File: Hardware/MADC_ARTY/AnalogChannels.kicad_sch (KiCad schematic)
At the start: 37 parts, among them Q1 MMBT6429, Q10 MMBF4392, Q11 MMBT6429, Q12 MMBT6429, Q2 JFE2140D, Q3 MMBT6429, Q4 MMBF4392, Q5 MMBT6429, Q6 MMBT6429, Q7 MMBT6429, Q8 JFE2140D, Q9 MMBT6429, U2 ADA4077-4ARUZ, U3 ADA4077-4ARUZ, U4 ADA4077-2xRMZ

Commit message: Schematic
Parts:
- removed RN1, RN2: MPMT4001AT1, Package_TO_SOT_SMD:SOT-23, symbol Device:VoltageDivider
- added RN1, RN2: MPMT4001AT1, Package_TO_SOT_SMD:SOT-23, symbol Device:VoltageDivider_CenterPin3
- renumbered U2 to U1, U3 to U2, U4 to U3
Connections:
- net at Q9.2 (E), R11.1, R9.1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: now also RN2.2
- net at R11.2, R12.2, R13.1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: now also RN2.3
- net at R4.2, R5.2, R6.1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: now also RN1.3
- net at Q11.2 (E), R13.2, R14.1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: now also RN2.1
- net at Q3.2 (E), R2.1, R4.1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: now also RN1.2
- net at Q5.2 (E), R6.2, R7.1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: now also RN1.1

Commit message: Schematic
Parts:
- removed U1, U2: ADA4077-4ARUZ, Package_SO:TSSOP-14_4.4x5mm_P0.65mm, symbol MADC_ARTY:ADA4077-4ARUZ
- removed U3: ADA4077-2xRMZ, Package_SO:MSOP-8_3x3mm_P0.65mm, symbol MADC_ARTY:ADA4077-2xRMZ
- added U1: OPA2192, Package_SO:VSSOP-8_3x3mm_P0.65mm, symbol Amplifier_Operational:OPA2197xDGK
- added U2, U3: OPA4192IPW, Package_SO:TSSOP-14_4.4x5mm_P0.65mm, symbol Amplifier_Operational:OPA4196xPW
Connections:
- net GND: now also U1.3 (+), U1.5 (+)
- net OUT_N: now also U3.8
- net OUT_P: now also U2.8
- net at Q1.3 (C), Q2.1, Q3.3 (C): now also U2.10 (+), U2.12 (+)
- net at Q11.2 (E), R13.2, R14.1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: now also U3.6 (-)
- net at Q9.2 (E), R11.1, R9.1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: now also U3.2 (-)
- net at R11.2, R12.2, R13.1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: now also U1.7
- net at Q10.3 (G): now also U3.13 (-), U3.14
- net at R4.2, R5.2, R6.1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: now also U1.1
- net at R1.2, R3.1: now also U1.2 (-)
- net at Q11.3 (C), Q12.3 (C), Q8.5: now also U3.9 (-)
- net at R10.2, R12.1: now also U3.3 (+), U3.5 (+)
- net at Q12.1 (B): now also U3.7
- net at Q1.1 (B): now also U2.1
- net at Q3.2 (E), R2.1, R4.1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: now also U2.2 (-)
- net at R3.2, R5.1: now also U2.3 (+), U2.5 (+)
- net at R10.1, R8.2: now also U1.6 (-)
- net at Q2.5, Q5.3 (C), Q6.3 (C): now also U2.9 (-)
- net at Q5.2 (E), R6.2, R7.1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: now also U2.6 (-)
- net at Q4.3 (G): now also U2.13 (-), U2.14
- net at Q6.1 (B): now also U2.7
- net at Q7.3 (C), Q8.1, Q9.3 (C): now also U3.10 (+), U3.12 (+)
- net at Q7.1 (B): now also U3.1
- net VCC renamed +18V
- net +18V: now also U1.8 (V+), U2.4 (V+), U3.4 (V+)
- net VEE renamed -18V
- net -18V: now also U1.4 (V-), U2.11 (V-), U3.11 (V-)

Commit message: Schematic
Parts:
- added unit 3 of Q8
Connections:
- no-connect marks 2 -> 4
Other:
- moved on the sheet: C1, C2, C3, C4, C5, C6, Q2C, U2E, U3E

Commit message: PCB and Schematic
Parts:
- removed C1, C4: 0.1u, Capacitor_SMD:C_0603_1608Metric, symbol Device:C
- removed Q10: MMBF4392, Package_TO_SOT_SMD:SOT-23, symbol Transistor_FET:MMBF4392
- removed Q11, Q12, Q7, Q9: MMBT6429, Package_TO_SOT_SMD:SOT-23, symbol Transistor_BJT:Q_NPN_BEC
- removed Q8: JFE2140D, Package_SO:SOIC-8_3.9x4.9mm_P1.27mm, symbol Transistor_FET:JFE2140D
- removed R10, R14, R9: 21k5/0.125W, Resistor_SMD:R_0603_1608Metric, symbol Device:R
- removed R11, R12, R13: 2k/0.1%, Resistor_SMD:R_0603_1608Metric, symbol Device:R
- removed RN2: MPMT4001AT1, Package_TO_SOT_SMD:SOT-23, symbol Device:VoltageDivider_CenterPin3
- removed U3: OPA4192IPW, Package_SO:TSSOP-14_4.4x5mm_P0.65mm, symbol Amplifier_Operational:OPA4196xPW
- added R3, R5: 0, Resistor_SMD:R_0603_1608Metric, symbol Device:R
- added TP19, TP21, TP23, TP25, TP27: TestPoint, symbol Connector:TestPoint
- R8: value 14k7 -> 0
- renumbered C2 to C1, C3 to C2, C5 to C3, C6 to C4, Q2 to Q1, Q1 to Q2, R7 to R10, R3 to R4, R4 to R6, R5 to R7, R6 to R9
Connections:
- net +10V: no longer R8.1
- net at Q1.1, Q2.3 (C), Q3.3 (C)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: now also TP21.1
- net at Q1.2, Q1.6, Q4.2 (S): now also TP19.1
- net at U1.7: now also R8.2, R5.2
- net at U1.6 (-): now also R3.2, R5.1; no longer R8.2
- net at R6.2, R7.2, R9.1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: now also R8.1, TP27.1
- net at R1.2, R4.1, U1.2 (-): now also R3.1
- net IN_P renamed IN
- net IN: now also TP25.1
- net OUT_P renamed OUT
- net OUT: now also TP23.1
- no-connect marks 4 -> 2
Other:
- moved on the sheet: C1, C2, C3, C4, Q1A, Q1B, Q1C, Q2, Q3, Q4, Q5, Q6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

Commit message: PCB
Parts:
- TP1: renamed from TP25; footprint (none) -> TestPoint:TestPoint_Pad_D2.0mm
- TP2: renamed from TP19; footprint (none) -> TestPoint:TestPoint_Pad_D2.0mm
- TP3: renamed from TP21; footprint (none) -> TestPoint:TestPoint_Pad_D2.0mm
- TP4: renamed from TP27; footprint (none) -> TestPoint:TestPoint_Pad_D2.0mm
- TP5: renamed from TP23; footprint (none) -> TestPoint:TestPoint_Pad_D2.0mm

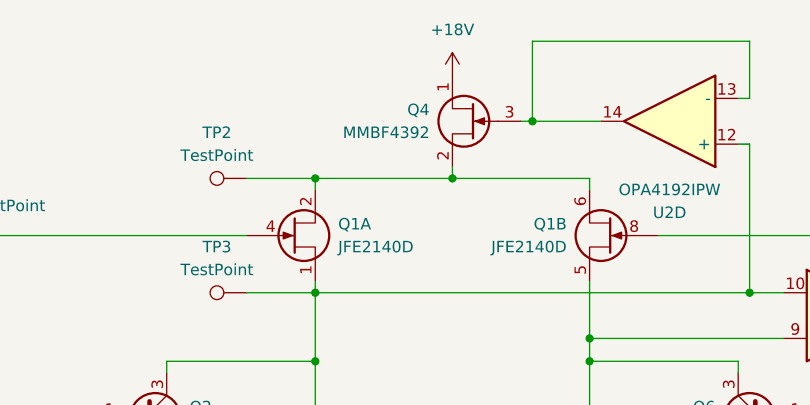
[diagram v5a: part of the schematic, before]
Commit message: MADC module send to production
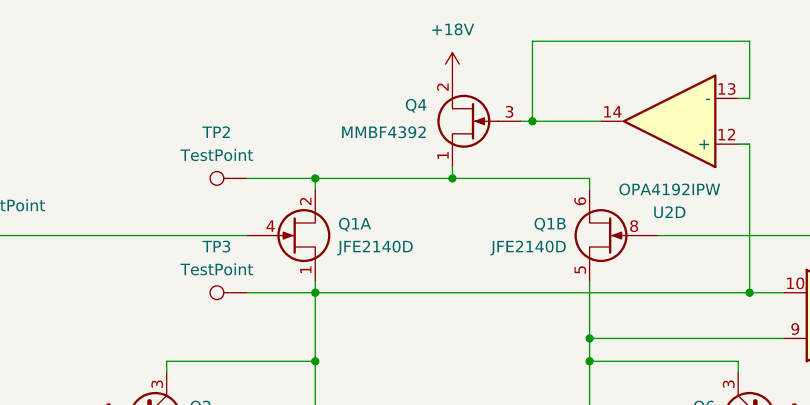
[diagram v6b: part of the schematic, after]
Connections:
- net +18V: now also Q4.2 (S); no longer Q4.1 (D)
- net at Q1.2, Q1.6, TP2.1: now also Q4.1 (D); no longer Q4.2 (S)
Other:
- moved on the sheet: Q4
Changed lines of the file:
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@@
 			(project "MADC_ARTY"
 				(path "/eadab778-ea7c-433e-b0bd-0d0c238907e0/37dfacfc-f3f5-4a09-9e7e-ab0b8ea302f6/3691a135-d759-4453-b099-98c35d021fc0"
-					(reference "#PWR0162")
+					(reference "#PWR0126")
 					(unit 1)
 				)
@@
 			(project "MADC_ARTY"
 				(path "/eadab778-ea7c-433e-b0bd-0d0c238907e0/37dfacfc-f3f5-4a09-9e7e-ab0b8ea302f6/3691a135-d759-4453-b099-98c35d021fc0"
-					(reference "R70")
+					(reference "R57")
 					(unit 1)
 				)
@@
 			(project "MADC_ARTY"
 				(path "/eadab778-ea7c-433e-b0bd-0d0c238907e0/37dfacfc-f3f5-4a09-9e7e-ab0b8ea302f6/3691a135-d759-4453-b099-98c35d021fc0"
-					(reference "TP37")
+					(reference "TP31")
 					(unit 1)
 				)
@@
 			(project "MADC_ARTY"
 				(path "/eadab778-ea7c-433e-b0bd-0d0c238907e0/37dfacfc-f3f5-4a09-9e7e-ab0b8ea302f6/3691a135-d759-4453-b099-98c35d021fc0"
-					(reference "U28")
+					(reference "U20")
 					(unit 3)
 				)
@@
 			(project "MADC_ARTY"
 				(path "/eadab778-ea7c-433e-b0bd-0d0c238907e0/37dfacfc-f3f5-4a09-9e7e-ab0b8ea302f6/3691a135-d759-4453-b099-98c35d021fc0"
-					(reference "R78")
+					(reference "R65")
 					(unit 1)
 				)
@@
 			(project "MADC_ARTY"
 				(path "/eadab778-ea7c-433e-b0bd-0d0c238907e0/37dfacfc-f3f5-4a09-9e7e-ab0b8ea302f6/3691a135-d759-4453-b099-98c35d021fc0"
-					(reference "C66")
+					(reference "C46")
 					(unit 1)
 				)
@@
 			(project "MADC_ARTY"
 				(path "/eadab778-ea7c-433e-b0bd-0d0c238907e0/37dfacfc-f3f5-4a09-9e7e-ab0b8ea302f6/3691a135-d759-4453-b099-98c35d021fc0"
-					(reference "#PWR0161")
+					(reference "#PWR0125")
 					(unit 1)
 				)
@@
 			(project "MADC_ARTY"
 				(path "/eadab778-ea7c-433e-b0bd-0d0c238907e0/37dfacfc-f3f5-4a09-9e7e-ab0b8ea302f6/3691a135-d759-4453-b099-98c35d021fc0"
-					(reference "#PWR0160")
+					(reference "#PWR0124")
 					(unit 1)
 				)
@@
 			(project "MADC_ARTY"
 				(path "/eadab778-ea7c-433e-b0bd-0d0c238907e0/37dfacfc-f3f5-4a09-9e7e-ab0b8ea302f6/3691a135-d759-4453-b099-98c35d021fc0"
-					(reference "R77")
+					(reference "R64")
 					(unit 1)
 				)
@@
 			(project "MADC_ARTY"
 				(path "/eadab778-ea7c-433e-b0bd-0d0c238907e0/37dfacfc-f3f5-4a09-9e7e-ab0b8ea302f6/3691a135-d759-4453-b099-98c35d021fc0"
-					(reference "TP36")
+					(reference "TP30")
 					(unit 1)
 				)
@@
 			(project "MADC_ARTY"
 				(path "/eadab778-ea7c-433e-b0bd-0d0c238907e0/37dfacfc-f3f5-4a09-9e7e-ab0b8ea302f6/3691a135-d759-4453-b099-98c35d021fc0"
-					(reference "TP35")
+					(reference "TP29")
 					(unit 1)
 				)
@@
 			(project "MADC_ARTY"
 				(path "/eadab778-ea7c-433e-b0bd-0d0c238907e0/37dfacfc-f3f5-4a09-9e7e-ab0b8ea302f6/3691a135-d759-4453-b099-98c35d021fc0"
-					(reference "U27")
+					(reference "U19")
 					(unit 3)
 				)
@@
 			(project "MADC_ARTY"
 				(path "/eadab778-ea7c-433e-b0bd-0d0c238907e0/37dfacfc-f3f5-4a09-9e7e-ab0b8ea302f6/3691a135-d759-4453-b099-98c35d021fc0"
-					(reference "#PWR0167")
+					(reference "#PWR0131")
 					(unit 1)
 				)
@@
 			(project "MADC_ARTY"
 				(path "/eadab778-ea7c-433e-b0bd-0d0c238907e0/37dfacfc-f3f5-4a09-9e7e-ab0b8ea302f6/3691a135-d759-4453-b099-98c35d021fc0"
-					(reference "R75")
+					(reference "R62")
 					(unit 1)
 				)
@@
 			(project "MADC_ARTY"
 				(path "/eadab778-ea7c-433e-b0bd-0d0c238907e0/37dfacfc-f3f5-4a09-9e7e-ab0b8ea302f6/3691a135-d759-4453-b099-98c35d021fc0"
-					(reference "RN2")
+					(reference "RN3")
 					(unit 1)
 				)
@@
 	(symbol
 		(lib_id "Transistor_FET:MMBF4392")
-		(at 156.21 35.56 0)
-		(mirror y)
+		(at 156.21 35.56 180)
 		(unit 1)
 		(exclude_from_sim no)
@@
 		(dnp no)
 		(property "Reference" "Q4"
-			(at 151.13 34.2899 0)
+			(at 150.876 33.782 0)
 			(effects
 				(font
@@
 		)
 		(property "Value" "MMBF4392"
-			(at 151.13 36.8299 0)
+			(at 150.876 36.83 0)
 			(effects
 				(font
@@
 		)
 		(property "Footprint" "Package_TO_SOT_SMD:SOT-23"
-			(at 151.13 37.465 0)
+			(at 151.13 33.655 0)
 			(effects
 				(font
@@
 		)
 		(property "Datasheet" "https://www.onsemi.com/pub/Collateral/MMBF4391LT1-D.PDF"
-			(at 151.13 39.37 0)
+			(at 151.13 31.75 0)
 			(effects
 				(font
@@
 			(project "MADC_ARTY"
 				(path "/eadab778-ea7c-433e-b0bd-0d0c238907e0/37dfacfc-f3f5-4a09-9e7e-ab0b8ea302f6/3691a135-d759-4453-b099-98c35d021fc0"
-					(reference "U28")
+					(reference "U20")
 					(unit 5)
 				)
@@
 			(project "MADC_ARTY"
 				(path "/eadab778-ea7c-433e-b0bd-0d0c238907e0/37dfacfc-f3f5-4a09-9e7e-ab0b8ea302f6/3691a135-d759-4453-b099-98c35d021fc0"
-					(reference "#PWR0163")
+					(reference "#PWR0127")
 					(unit 1)
 				)
@@
 			(project "MADC_ARTY"
 				(path "/eadab778-ea7c-433e-b0bd-0d0c238907e0/37dfacfc-f3f5-4a09-9e7e-ab0b8ea302f6/3691a135-d759-4453-b099-98c35d021fc0"
-					(reference "R69")
+					(reference "R56")
 					(unit 1)
 				)
@@
 			(project "MADC_ARTY"
 				(path "/eadab778-ea7c-433e-b0bd-0d0c238907e0/37dfacfc-f3f5-4a09-9e7e-ab0b8ea302f6/3691a135-d759-4453-b099-98c35d021fc0"
-					(reference "#PWR0164")
+					(reference "#PWR0128")
 					(unit 1)
 				)
@@
 			(project "MADC_ARTY"
 				(path "/eadab778-ea7c-433e-b0bd-0d0c238907e0/37dfacfc-f3f5-4a09-9e7e-ab0b8ea302f6/3691a135-d759-4453-b099-98c35d021fc0"
-					(reference "U27")
+					(reference "U19")
 					(unit 2)
 				)
@@
 			(project "MADC_ARTY"
 				(path "/eadab778-ea7c-433e-b0bd-0d0c238907e0/37dfacfc-f3f5-4a09-9e7e-ab0b8ea302f6/3691a135-d759-4453-b099-98c35d021fc0"
-					(reference "TP33")
+					(reference "TP27")
 					(unit 1)
 				)
@@
 			(project "MADC_ARTY"
 				(path "/eadab778-ea7c-433e-b0bd-0d0c238907e0/37dfacfc-f3f5-4a09-9e7e-ab0b8ea302f6/3691a135-d759-4453-b099-98c35d021fc0"
-					(reference "#PWR0157")
+					(reference "#PWR0121")
 					(unit 1)
 				)
@@
 			(project "MADC_ARTY"
 				(path "/eadab778-ea7c-433e-b0bd-0d0c238907e0/37dfacfc-f3f5-4a09-9e7e-ab0b8ea302f6/3691a135-d759-4453-b099-98c35d021fc0"
-					(reference "U28")
+					(reference "U20")
 					(unit 1)
 				)
@@
 			(project "MADC_ARTY"
 				(path "/eadab778-ea7c-433e-b0bd-0d0c238907e0/37dfacfc-f3f5-4a09-9e7e-ab0b8ea302f6/3691a135-d759-4453-b099-98c35d021fc0"
-					(reference "R71")
+					(reference "R58")
 					(unit 1)
 				)
@@
 			(project "MADC_ARTY"
 				(path "/eadab778-ea7c-433e-b0bd-0d0c238907e0/37dfacfc-f3f5-4a09-9e7e-ab0b8ea302f6/3691a135-d759-4453-b099-98c35d021fc0"
-					(reference "TP34")
+					(reference "TP28")
 					(unit 1)
 				)
@@
 			(project "MADC_ARTY"
 				(path "/eadab778-ea7c-433e-b0bd-0d0c238907e0/37dfacfc-f3f5-4a09-9e7e-ab0b8ea302f6/3691a135-d759-4453-b099-98c35d021fc0"
-					(reference "#PWR0158")
+					(reference "#PWR0122")
 					(unit 1)
 				)
@@
 			(project "MADC_ARTY"
 				(path "/eadab778-ea7c-433e-b0bd-0d0c238907e0/37dfacfc-f3f5-4a09-9e7e-ab0b8ea302f6/3691a135-d759-4453-b099-98c35d021fc0"
-					(reference "C65")
+					(reference "C45")
 					(unit 1)
 				)
@@
 			(project "MADC_ARTY"
 				(path "/eadab778-ea7c-433e-b0bd-0d0c238907e0/37dfacfc-f3f5-4a09-9e7e-ab0b8ea302f6/3691a135-d759-4453-b099-98c35d021fc0"
-					(reference "U28")
+					(reference "U20")
 					(unit 2)
 				)
@@
 			(project "MADC_ARTY"
 				(path "/eadab778-ea7c-433e-b0bd-0d0c238907e0/37dfacfc-f3f5-4a09-9e7e-ab0b8ea302f6/3691a135-d759-4453-b099-98c35d021fc0"
-					(reference "R72")
+					(reference "R59")
 					(unit 1)
 				)
@@
 			(project "MADC_ARTY"
 				(path "/eadab778-ea7c-433e-b0bd-0d0c238907e0/37dfacfc-f3f5-4a09-9e7e-ab0b8ea302f6/3691a135-d759-4453-b099-98c35d021fc0"
-					(reference "#PWR0166")
+					(reference "#PWR0130")
 					(unit 1)
 				)
@@
 			(project "MADC_ARTY"
 				(path "/eadab778-ea7c-433e-b0bd-0d0c238907e0/37dfacfc-f3f5-4a09-9e7e-ab0b8ea302f6/3691a135-d759-4453-b099-98c35d021fc0"
-					(reference "#PWR0165")
+					(reference "#PWR0129")
 					(unit 1)
 				)
@@
 			(project "MADC_ARTY"
 				(path "/eadab778-ea7c-433e-b0bd-0d0c238907e0/37dfacfc-f3f5-4a09-9e7e-ab0b8ea302f6/3691a135-d759-4453-b099-98c35d021fc0"
-					(reference "U27")
+					(reference "U19")
 					(unit 1)
 				)
@@
 			(project "MADC_ARTY"
 				(path "/eadab778-ea7c-433e-b0bd-0d0c238907e0/37dfacfc-f3f5-4a09-9e7e-ab0b8ea302f6/3691a135-d759-4453-b099-98c35d021fc0"
-					(reference "C64")
+					(reference "C44")
 					(unit 1)
 				)
@@
 			(project "MADC_ARTY"
 				(path "/eadab778-ea7c-433e-b0bd-0d0c238907e0/37dfacfc-f3f5-4a09-9e7e-ab0b8ea302f6/3691a135-d759-4453-b099-98c35d021fc0"
-					(reference "R76")
+					(reference "R63")
 					(unit 1)
 				)
@@
 			(project "MADC_ARTY"
 				(path "/eadab778-ea7c-433e-b0bd-0d0c238907e0/37dfacfc-f3f5-4a09-9e7e-ab0b8ea302f6/3691a135-d759-4453-b099-98c35d021fc0"
-					(reference "#PWR0168")
+					(reference "#PWR0132")
 					(unit 1)
 				)
@@
 			(project "MADC_ARTY"
 				(path "/eadab778-ea7c-433e-b0bd-0d0c238907e0/37dfacfc-f3f5-4a09-9e7e-ab0b8ea302f6/3691a135-d759-4453-b099-98c35d021fc0"
-					(reference "#PWR0159")
+					(reference "#PWR0123")
 					(unit 1)
 				)
@@
 			(project "MADC_ARTY"
 				(path "/eadab778-ea7c-433e-b0bd-0d0c238907e0/37dfacfc-f3f5-4a09-9e7e-ab0b8ea302f6/3691a135-d759-4453-b099-98c35d021fc0"
-					(reference "R73")
+					(reference "R60")
 					(unit 1)
 				)
@@
 			(project "MADC_ARTY"
 				(path "/eadab778-ea7c-433e-b0bd-0d0c238907e0/37dfacfc-f3f5-4a09-9e7e-ab0b8ea302f6/3691a135-d759-4453-b099-98c35d021fc0"
-					(reference "C67")
+					(reference "C47")
 					(unit 1)
 				)
@@
 			(project "MADC_ARTY"
 				(path "/eadab778-ea7c-433e-b0bd-0d0c238907e0/37dfacfc-f3f5-4a09-9e7e-ab0b8ea302f6/3691a135-d759-4453-b099-98c35d021fc0"
-					(reference "R74")
+					(reference "R61")
 					(unit 1)
 				)
@@
 			(project "MADC_ARTY"
 				(path "/eadab778-ea7c-433e-b0bd-0d0c238907e0/37dfacfc-f3f5-4a09-9e7e-ab0b8ea302f6/3691a135-d759-4453-b099-98c35d021fc0"
-					(reference "U28")
+					(reference "U20")
 					(unit 4)
 				)

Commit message: PCB and schematic
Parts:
- Q4: value MMBF4392 -> MMBF4392LT1G
- TP1, TP2, TP3, TP4, TP5: now left out of the parts list
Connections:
- net +18V: now also Q4.1 (D); no longer Q4.2 (S)
- net at Q1.2, Q1.6, TP2.1: now also Q4.2 (S); no longer Q4.1 (D)
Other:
- moved on the sheet: Q4
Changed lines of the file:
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@@
 		(dnp no)
 		(fields_autoplaced yes)
-		(property "Reference" "#PWR06"
+		(property "Reference" "#PWR6"
 			(at 69.85 193.04 0)
 			(effects
@@
 			(project "MADC_ARTY"
 				(path "/eadab778-ea7c-433e-b0bd-0d0c238907e0/37dfacfc-f3f5-4a09-9e7e-ab0b8ea302f6/3691a135-d759-4453-b099-98c35d021fc0"
-					(reference "#PWR0126")
-					(unit 1)
-				)
-				(path "/eadab778-ea7c-433e-b0bd-0d0c238907e0/37dfacfc-f3f5-4a09-9e7e-ab0b8ea302f6/b2131341-7d85-419f-a559-e014f1324d0f"
-					(reference "#PWR06")
+					(reference "#PWR126")
+					(unit 1)
+				)
+				(path "/eadab778-ea7c-433e-b0bd-0d0c238907e0/37dfacfc-f3f5-4a09-9e7e-ab0b8ea302f6/b2131341-7d85-419f-a559-e014f1324d0f"
+					(reference "#PWR6")
 					(unit 1)
 				)
@@
 		(unit 1)
 		(exclude_from_sim no)
-		(in_bom yes)
+		(in_bom no)
 		(on_board yes)
 		(dnp no)
@@
 		(unit 1)
 		(exclude_from_sim no)
-		(in_bom yes)
+		(in_bom no)
 		(on_board yes)
 		(dnp no)
@@
 		(unit 1)
 		(exclude_from_sim no)
-		(in_bom yes)
+		(in_bom no)
 		(on_board yes)
 		(dnp no)
@@
 		(on_board yes)
 		(dnp no)
-		(property "Reference" "#PWR011"
+		(property "Reference" "#PWR11"
 			(at 127 143.51 0)
 			(effects
@@
 		)
 		(property "Value" "GND"
-			(at 130.302 143.51 90)
-			(effects
-				(font
-					(size 1.27 1.27)
-				)
-				(justify right)
+			(at 129.54 143.51 0)
+			(effects
+				(font
+					(size 1.27 1.27)
+				)
 			)
 		)
@@
 			(project "MADC_ARTY"
 				(path "/eadab778-ea7c-433e-b0bd-0d0c238907e0/37dfacfc-f3f5-4a09-9e7e-ab0b8ea302f6/3691a135-d759-4453-b099-98c35d021fc0"
-					(reference "#PWR0131")
-					(unit 1)
-				)
-				(path "/eadab778-ea7c-433e-b0bd-0d0c238907e0/37dfacfc-f3f5-4a09-9e7e-ab0b8ea302f6/b2131341-7d85-419f-a559-e014f1324d0f"
-					(reference "#PWR011")
+					(reference "#PWR131")
+					(unit 1)
+				)
+				(path "/eadab778-ea7c-433e-b0bd-0d0c238907e0/37dfacfc-f3f5-4a09-9e7e-ab0b8ea302f6/b2131341-7d85-419f-a559-e014f1324d0f"
+					(reference "#PWR11")
 					(unit 1)
 				)
@@
 	(symbol
 		(lib_id "Transistor_FET:MMBF4392")
-		(at 156.21 35.56 180)
+		(at 156.21 35.56 0)
+		(mirror y)
 		(unit 1)
 		(exclude_from_sim no)
@@
 		(dnp no)
 		(property "Reference" "Q4"
-			(at 150.876 33.782 0)
-			(effects
-				(font
-					(size 1.27 1.27)
-				)
-				(justify left)
-			)
-		)
-		(property "Value" "MMBF4392"
-			(at 150.876 36.83 0)
+			(at 150.368 33.782 0)
+			(effects
+				(font
+					(size 1.27 1.27)
+				)
+				(justify left)
+			)
+		)
+		(property "Value" "MMBF4392LT1G"
+			(at 150.622 36.83 0)
 			(effects
 				(font
@@
 		)
 		(property "Footprint" "Package_TO_SOT_SMD:SOT-23"
-			(at 151.13 33.655 0)
+			(at 151.13 37.465 0)
 			(effects
 				(font
@@
 		)
 		(property "Datasheet" "https://www.onsemi.com/pub/Collateral/MMBF4391LT1-D.PDF"
-			(at 151.13 31.75 0)
+			(at 151.13 39.37 0)
 			(effects
 				(font
@@
 		(dnp no)
 		(fields_autoplaced yes)
-		(property "Reference" "#PWR08"
+		(property "Reference" "#PWR8"
 			(at 92.71 193.04 0)
 			(effects
@@
 			(project "MADC_ARTY"
 				(path "/eadab778-ea7c-433e-b0bd-0d0c238907e0/37dfacfc-f3f5-4a09-9e7e-ab0b8ea302f6/3691a135-d759-4453-b099-98c35d021fc0"
-					(reference "#PWR0128")
-					(unit 1)
-				)
-				(path "/eadab778-ea7c-433e-b0bd-0d0c238907e0/37dfacfc-f3f5-4a09-9e7e-ab0b8ea302f6/b2131341-7d85-419f-a559-e014f1324d0f"
-					(reference "#PWR08")
+					(reference "#PWR128")
+					(unit 1)
+				)
+				(path "/eadab778-ea7c-433e-b0bd-0d0c238907e0/37dfacfc-f3f5-4a09-9e7e-ab0b8ea302f6/b2131341-7d85-419f-a559-e014f1324d0f"
+					(reference "#PWR8")
 					(unit 1)
 				)
@@
 		(unit 1)
 		(exclude_from_sim no)
-		(in_bom yes)
+		(in_bom no)
 		(on_board yes)
 		(dnp no)
@@
 		(unit 1)
 		(exclude_from_sim no)
-		(in_bom yes)
+		(in_bom no)
 		(on_board yes)
 		(dnp no)
@@
 		(on_board yes)
 		(dnp no)
-		(property "Reference" "#PWR010"
+		(property "Reference" "#PWR10"
 			(at 127 125.73 0)
 			(effects
@@
 		)
 		(property "Value" "GND"
-			(at 130.302 125.73 90)
-			(effects
-				(font
-					(size 1.27 1.27)
-				)
-				(justify right)
+			(at 129.54 125.73 0)
+			(effects
+				(font
+					(size 1.27 1.27)
+				)
 			)
 		)
@@
 			(project "MADC_ARTY"
 				(path "/eadab778-ea7c-433e-b0bd-0d0c238907e0/37dfacfc-f3f5-4a09-9e7e-ab0b8ea302f6/3691a135-d759-4453-b099-98c35d021fc0"
-					(reference "#PWR0130")
-					(unit 1)
-				)
-				(path "/eadab778-ea7c-433e-b0bd-0d0c238907e0/37dfacfc-f3f5-4a09-9e7e-ab0b8ea302f6/b2131341-7d85-419f-a559-e014f1324d0f"
-					(reference "#PWR010")
-					(unit 1)
-				)
+					(reference "#PWR130")
+					(unit 1)
+				)
+				(path "/eadab778-ea7c-433e-b0bd-0d0c238907e0/37dfacfc-f3f5-4a09-9e7e-ab0b8ea302f6/b2131341-7d85-419f-a559-e014f1324d0f"
+					(reference "#PWR10")
+					(unit 1)
+				)

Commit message: BOM
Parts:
- Q2, Q3, Q5, Q6: value MMBT6429 -> MMBT6429LT1G
- U1: value OPA2192 -> OPA2192IDGKT
